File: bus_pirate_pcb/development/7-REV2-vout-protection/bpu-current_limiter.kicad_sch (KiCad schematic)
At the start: 34 parts, among them Q601 MMDT3906DW, Q602 BC2301T 2.8A, U403 AP2127K-ADJ, U5 GS358-FR, U601 GS321A-TR, U602 GSV331-TR

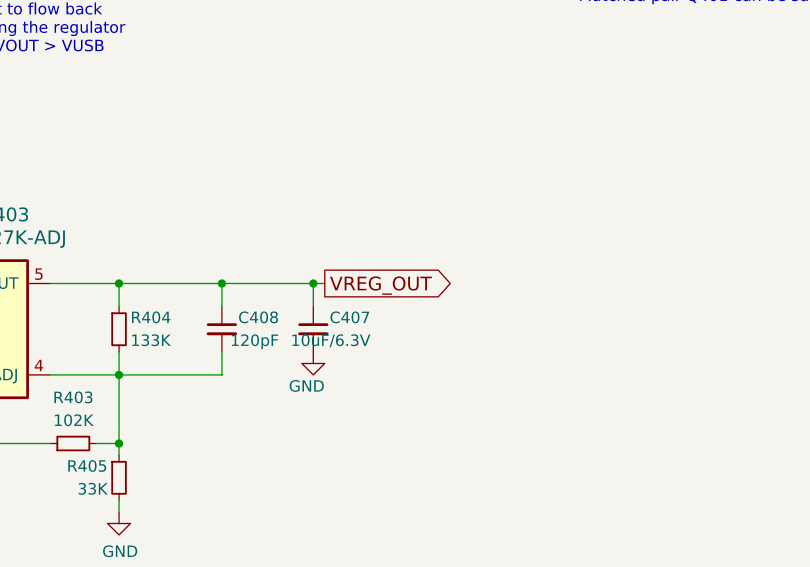
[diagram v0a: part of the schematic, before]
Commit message: 7R2 with vout protection
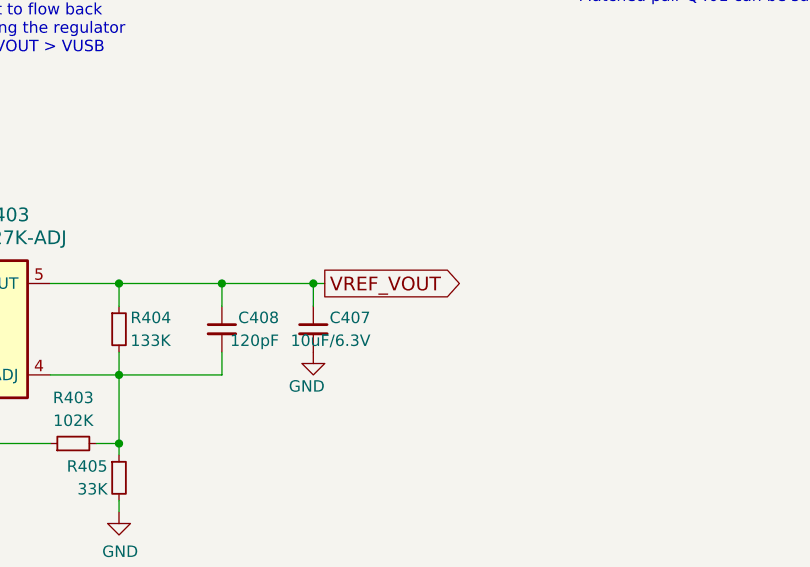
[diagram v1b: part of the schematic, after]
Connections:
- net VREG_OUT renamed VREF_VOUT
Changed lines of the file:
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@@
+		)
+	)
+	(global_label "VREF_VOUT"
+		(shape output)
+		(at 173.99 106.68 0)
+		(effects
+			(font
+				(size 1.524 1.524)
+			)
+			(justify left)
+		)
+		(property "Intersheetrefs" "${INTERSHEET_REFS}"
+			(at 173.99 106.68 90)
+			(effects
+				(font
+					(size 1.27 1.27)
+				)
+				(hide yes)
+			)
 		)
 	)
@@
 			(effects
 				(font
-					(size 1.27 1.27)
-				)
-				(hide yes)
-			)
-		)
-	)
-	(global_label "VREG_OUT"
-		(shape output)
-		(at 173.99 106.68 0)
-		(effects
-			(font
-				(size 1.524 1.524)
-			)
-			(justify left)
-		)
-		(property "Intersheetrefs" "${INTERSHEET_REFS}"
-			(at 173.99 106.68 0)
-			(effects
-				(font
